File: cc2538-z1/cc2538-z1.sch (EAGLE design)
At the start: 90 parts, among them J2 2-PIN-MOLEX, Q2 DMG6602SVT, U1 CC2538, U2 CC1120_RHM_32, U3 TPD2E001IDRLRQ1, U4 CP2103, U5 BSS138PS, U6 BSS138PS, U7 BSS138PS, X1 FA-128, X2 32MHz, X3 32.768K

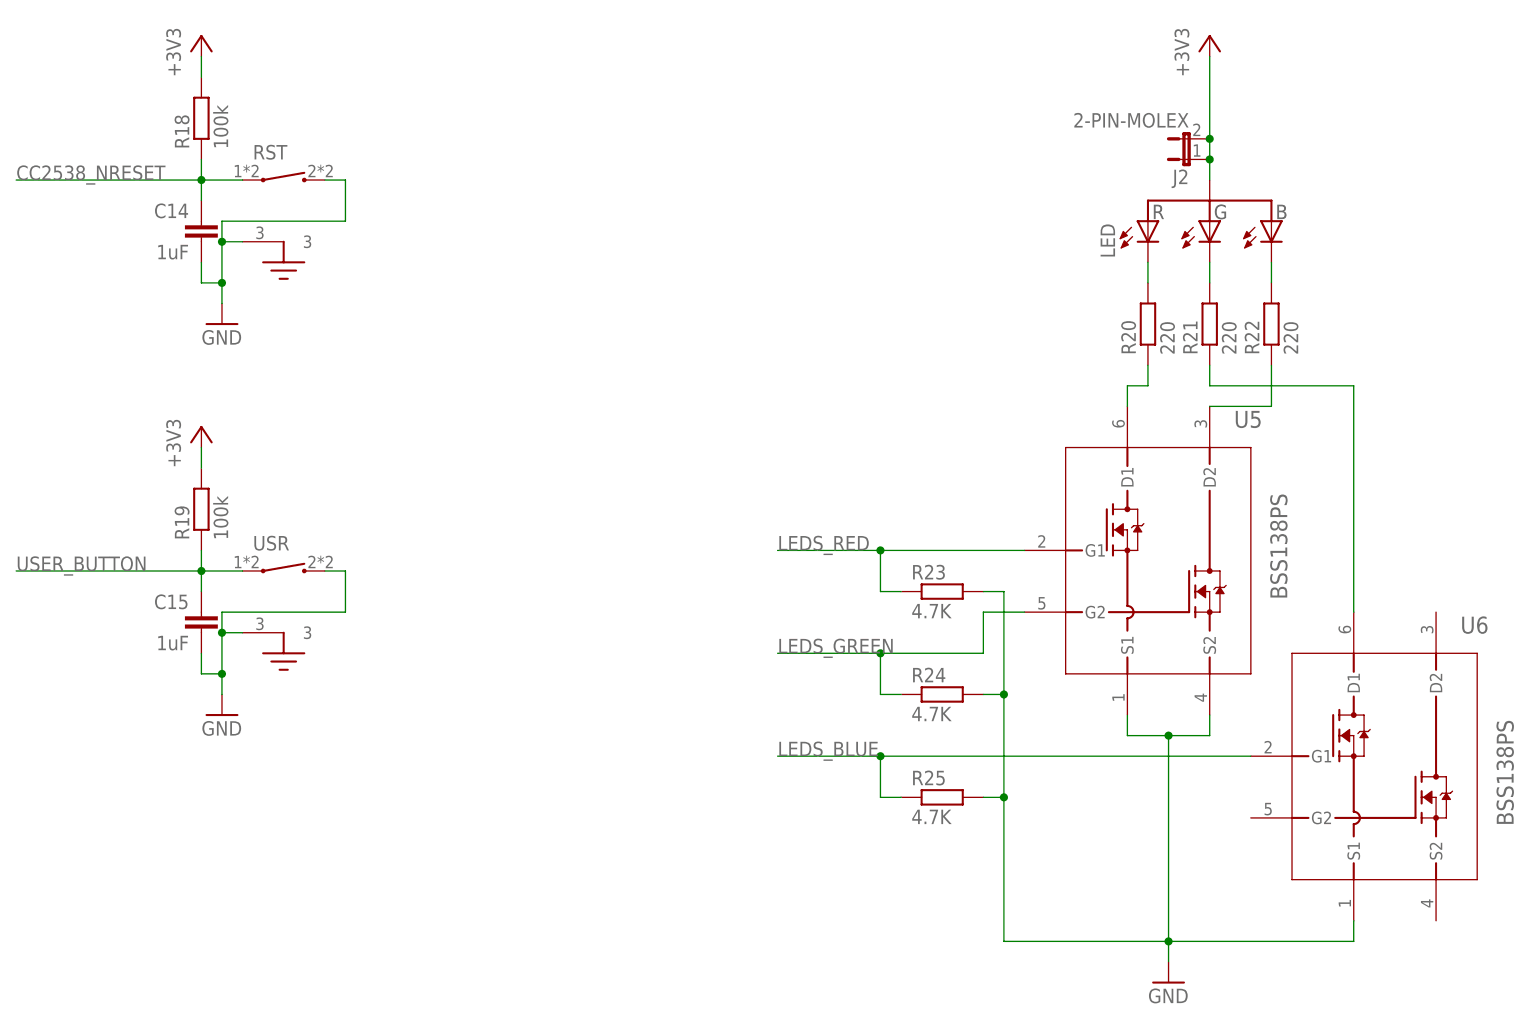
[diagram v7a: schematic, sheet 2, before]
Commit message: Moved to a 4-layer board.
Updated DRU to meet Euro Circuits Class 6C pool service.

22 airwires left

TODO: Check SD card SEL implementation.
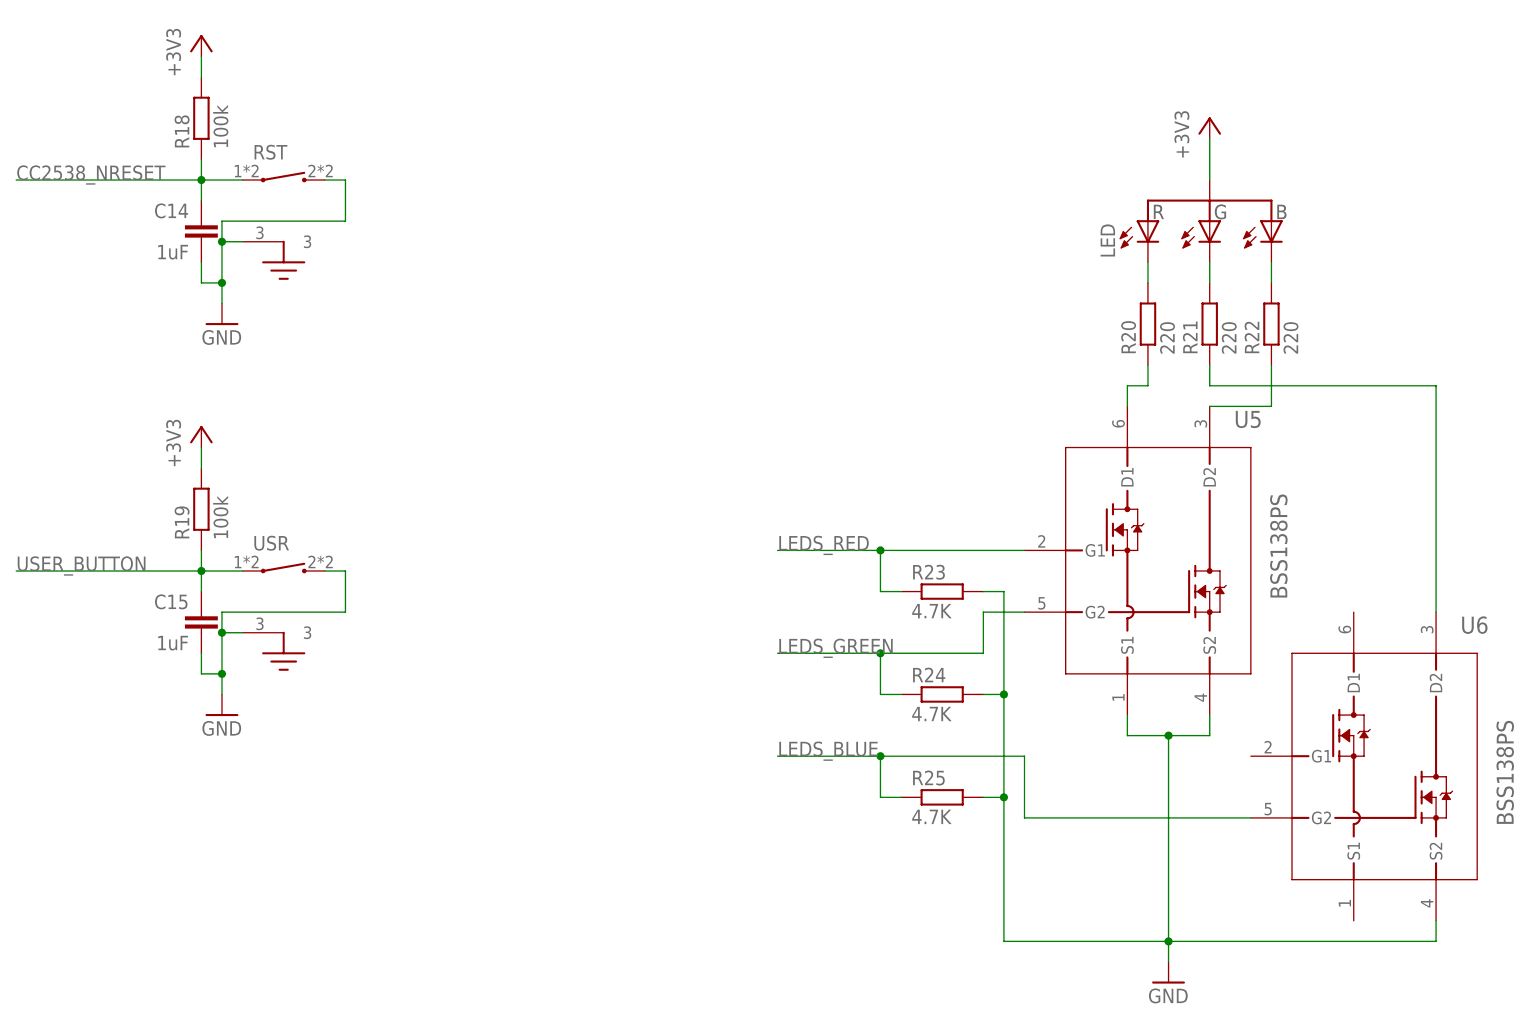
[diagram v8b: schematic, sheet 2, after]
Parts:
- removed J2: 2-PIN-MOLEX, farnell-parts:2-PIN-MOLEX
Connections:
- net +3V3: no longer J2.1, J2.2
- net GND: now also U6.S2; no longer U6.S1
- net LEDS_BLUE: now also U6.G2; no longer U6.G1
- net N$32: now also U6.D2; no longer U6.D1
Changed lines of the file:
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@@
 <part name="R21" library="rcl" deviceset="R-EU_" device="R0603" value="220"/>
 <part name="R22" library="rcl" deviceset="R-EU_" device="R0603" value="220"/>
-<part name="J2" library="farnell-parts" deviceset="2-PIN-MOLEX" device=""/>
 <part name="+3V10" library="supply1" deviceset="+3V3" device=""/>
 <part name="GND22" library="supply1" deviceset="GND" device=""/>
@@
 <instance part="R21" gate="G$1" x="71.12" y="12.7" rot="R90"/>
 <instance part="R22" gate="G$1" x="78.74" y="12.7" rot="R90"/>
-<instance part="J2" gate="G$1" x="68.58" y="33.02" rot="R90"/>
-<instance part="+3V10" gate="G$1" x="71.12" y="48.26"/>
+<instance part="+3V10" gate="G$1" x="71.12" y="38.1"/>
 <instance part="GND22" gate="1" x="66.04" y="-68.58"/>
 <instance part="R23" gate="G$1" x="38.1" y="-20.32"/>
@@
 <junction x="45.72" y="-33.02"/>
 <junction x="45.72" y="-45.72"/>
-<pinref part="U6" gate="A" pin="S1"/>
-<wire x1="88.9" y1="-60.96" x2="88.9" y2="-63.5" width="0.1524" layer="91"/>
-<wire x1="88.9" y1="-63.5" x2="66.04" y2="-63.5" width="0.1524" layer="91"/>
+<wire x1="99.06" y1="-63.5" x2="66.04" y2="-63.5" width="0.1524" layer="91"/>
 <pinref part="U5" gate="A" pin="S2"/>
 <wire x1="71.12" y1="-35.56" x2="71.12" y2="-38.1" width="0.1524" layer="91"/>
@@
 <junction x="66.04" y="-38.1"/>
 <junction x="66.04" y="-63.5"/>
+<pinref part="U6" gate="A" pin="S2"/>
+<wire x1="99.06" y1="-63.5" x2="99.06" y2="-60.96" width="0.1524" layer="91"/>
 </segment>
 </net>
@@
 <net name="LEDS_BLUE" class="0">
 <segment>
-<wire x1="76.2" y1="-40.64" x2="30.48" y2="-40.64" width="0.1524" layer="91"/>
 <label x="17.78" y="-40.64" size="1.778" layer="95"/>
 <pinref part="R25" gate="G$1" pin="1"/>
@@
 <wire x1="33.02" y1="-45.72" x2="30.48" y2="-45.72" width="0.1524" layer="91"/>
 <wire x1="30.48" y1="-45.72" x2="30.48" y2="-40.64" width="0.1524" layer="91"/>
+<pinref part="U6" gate="A" pin="G2"/>
+<wire x1="76.2" y1="-48.26" x2="48.26" y2="-48.26" width="0.1524" layer="91"/>
+<wire x1="48.26" y1="-48.26" x2="48.26" y2="-40.64" width="0.1524" layer="91"/>
+<wire x1="48.26" y1="-40.64" x2="30.48" y2="-40.64" width="0.1524" layer="91"/>
 <junction x="30.48" y="-40.64"/>
-<pinref part="U6" gate="A" pin="G1"/>
 </segment>
 </net>
@@
 </segment>
 <segment>
-<pinref part="J2" gate="G$1" pin="2"/>
 <pinref part="LED" gate="A" pin="2"/>
-<wire x1="71.12" y1="30.48" x2="71.12" y2="33.02" width="0.1524" layer="91"/>
-<pinref part="J2" gate="G$1" pin="1"/>
-<wire x1="71.12" y1="35.56" x2="71.12" y2="33.02" width="0.1524" layer="91"/>
-<junction x="71.12" y="33.02"/>
-<junction x="71.12" y="35.56"/>
 <pinref part="+3V10" gate="G$1" pin="+3V3"/>
-<wire x1="71.12" y1="35.56" x2="71.12" y2="45.72" width="0.1524" layer="91"/>
+<wire x1="71.12" y1="30.48" x2="71.12" y2="35.56" width="0.1524" layer="91"/>
 </segment>
 </net>
@@
 <pinref part="R21" gate="G$1" pin="1"/>
 <wire x1="71.12" y1="7.62" x2="71.12" y2="5.08" width="0.1524" layer="91"/>
-<pinref part="U6" gate="A" pin="D1"/>
-<wire x1="71.12" y1="5.08" x2="88.9" y2="5.08" width="0.1524" layer="91"/>
-<wire x1="88.9" y1="5.08" x2="88.9" y2="-22.86" width="0.1524" layer="91"/>
-</segment>
-</net>
+<wire x1="71.12" y1="5.08" x2="99.06" y2="5.08" width="0.1524" layer="91"/>
+<pinref part="U6" gate="A" pin="D2"/>
+<wire x1="99.06" y1="5.08" x2="99.06" y2="-22.86" width="0.1524" layer="91"/>
+</segment>
+</net>
